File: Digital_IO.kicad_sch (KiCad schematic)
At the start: 27 parts, among them J1 MMCX, J10 MMCX, J11 MMCX, J12 MMCX, J13 MMCX, J14 MMCX, J15 MMCX, J16 MMCX, J2 MMCX, J3 MMCX, J4 MMCX, J5 MMCX, J6 MMCX, J7 MMCX, J8 MMCX, J9 MMCX, U45 TLV75901PDRV, U46 TLV75901PDRV

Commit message: Routed LVDS lines
- Routed LVDS lines
- Swapped some digital output pairs
- Properly connected the output enable signal for digital outputs in the schematic
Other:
- note removed: "TODO!: Need Level Translation through existing gate on u26/u27"
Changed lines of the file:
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@@
 		(comment 1 "SPDX-License-Identifier: CERN-OHL-S-2.0+")
 	)
-	(text "TODO!: Need Level Translation through existing gate\non u26/u27"
-		(exclude_from_sim no)
-		(at 115.062 72.39 0)
-		(effects
-			(font
-				(size 1.27 1.27)
-			)
-		)
-	)
 	(junction
 		(at 280.67 114.3)
@@
 	(wire
 		(pts
-			(xy 137.16 53.34) (xy 143.51 53.34)
+			(xy 59.69 161.29) (xy 59.69 158.75)
 		)
 		(stroke
@@
 		)
 	)
-	(wire
+	(bus
 		(pts
-			(xy 59.69 161.29) (xy 59.69 158.75)
+			(xy 43.18 83.82) (xy 43.18 86.36)
 		)
 		(stroke
@@
 		)
 	)
-	(bus
+	(wire
 		(pts
-			(xy 43.18 83.82) (xy 43.18 86.36)
+			(xy 175.26 91.44) (xy 181.61 91.44)
 		)
 		(stroke
@@
 	(wire
 		(pts
-			(xy 181.61 91.44) (xy 175.26 91.44)
+			(xy 175.26 92.71) (xy 173.99 92.71)
 		)
 		(stroke
@@
 		)
 	)
-	(wire
-		(pts
-			(xy 92.71 53.34) (xy 92.71 68.58)
-		)
-		(stroke
-			(width 0)
-			(type default)
-		)
-	)
 	(bus
 		(pts
@@
 	(wire
 		(pts
-			(xy 92.71 68.58) (xy 137.16 68.58)
+			(xy 224.79 44.45) (xy 243.84 44.45)
 		)
 		(stroke
@@
 	(wire
 		(pts
-			(xy 224.79 44.45) (xy 243.84 44.45)
+			(xy 162.56 25.4) (xy 181.61 25.4)
 		)
 		(stroke
@@
 	(wire
 		(pts
-			(xy 162.56 25.4) (xy 181.61 25.4)
+			(xy 30.48 16.51) (xy 64.77 16.51)
 		)
 		(stroke
@@
 	(wire
 		(pts
-			(xy 87.63 53.34) (xy 92.71 53.34)
+			(xy 30.48 19.05) (xy 64.77 19.05)
 		)
 		(stroke
@@
 	(wire
 		(pts
+			(xy 175.26 92.71) (xy 175.26 91.44)
+		)
+		(stroke
+			(width 0)
+			(type default)
+		)
+	)
+	(wire
+		(pts
 			(xy 64.77 40.64) (xy 45.72 40.64)
 		)
@@
 	(wire
 		(pts
-			(xy 137.16 53.34) (xy 137.16 68.58)
-		)
-		(stroke
-			(width 0)
-			(type default)
-		)
-	)
-	(wire
-		(pts
 			(xy 64.77 53.34) (xy 45.72 53.34)
 		)
@@
 		)
 	)
-	(label "OE"
-		(at 175.26 91.44 0)
+	(label "OE_A"
+		(at 64.77 16.51 180)
 		(effects
 			(font
 				(size 1.27 1.27)
 			)
-			(justify left bottom)
+			(justify right bottom)
 		)
 	)
@@
 		)
 	)
-	(label "OE"
+	(label "OE_B"
 		(at 237.49 57.15 0)
 		(effects
@@
 		)
 	)
+	(label "OE_A"
+		(at 175.26 38.1 0)
+		(effects
+			(font
+				(size 1.27 1.27)
+			)
+			(justify left bottom)
+		)
+	)
 	(label "D_Output6.N"
 		(at 64.77 55.88 180)
@@
 		)
 	)
-	(label "OE"
+	(label "OE_B"
 		(at 237.49 146.05 0)
 		(effects
@@
 		)
 	)
-	(label "OE"
+	(label "OE_B"
 		(at 237.49 92.71 0)
 		(effects
@@
 		)
 	)
-	(label "OE"
-		(at 175.26 127 0)
-		(effects
-			(font
-				(size 1.27 1.27)
-			)
-			(justify left bottom)
-		)
-	)
 	(label "VCC_B"
 		(at 236.22 17.78 0)
@@
 		)
 	)
-	(label "D_Output6.P"
-		(at 162.56 129.54 0)
+	(label "OE_A"
+		(at 173.99 92.71 0)
 		(effects
 			(font
@@
 		)
 	)
-	(label "OE"
-		(at 175.26 38.1 0)
+	(label "D_Output6.P"
+		(at 162.56 129.54 0)
 		(effects
 			(font
@@
 		)
 	)
-	(label "OE"
+	(label "OE_B"
 		(at 237.49 128.27 0)
 		(effects
@@
 		)
 	)
-	(label "OE"
-		(at 175.26 144.78 0)
-		(effects
-			(font
-				(size 1.27 1.27)
-			)
-			(justify left bottom)
-		)
-	)
 	(label "VCC_B"
 		(at 236.22 124.46 0)
@@
 		)
 	)
-	(label "OE"
-		(at 175.26 109.22 0)
-		(effects
-			(font
-				(size 1.27 1.27)
-			)
-			(justify left bottom)
-		)
-	)
 	(label "VCC_A"
 		(at 173.99 16.51 0)
@@
 		)
 	)
+	(label "OE_A"
+		(at 175.26 73.66 0)
+		(effects
+			(font
+				(size 1.27 1.27)
+			)
+			(justify left bottom)
+		)
+	)
 	(label "D_Output4.N"
 		(at 162.56 96.52 0)
@@
 		)
 	)
+	(label "OE_A"
+		(at 175.26 144.78 0)
+		(effects
+			(font
+				(size 1.27 1.27)
+			)
+			(justify left bottom)
+		)
+	)
 	(label "VCC_A"
 		(at 173.99 140.97 0)
@@
 		)
 	)
-	(label "OE"
-		(at 175.26 73.66 0)
-		(effects
-			(font
-				(size 1.27 1.27)
-			)
-			(justify left bottom)
-		)
-	)
 	(label "D_Output15.N"
 		(at 224.79 151.13 0)
@@
 		)
 	)
-	(label "OE"
+	(label "OE_B"
 		(at 237.49 110.49 0)
 		(effects
@@
 		)
 	)
-	(label "OE"
+	(label "OE_A"
 		(at 175.26 20.32 0)
 		(effects
@@
 		)
 	)
-	(label "OE"
-		(at 143.51 53.34 180)
+	(label "OE_B"
+		(at 64.77 19.05 180)
 		(effects
 			(font
@@
 		)
 	)
+	(label "OE_A"
+		(at 175.26 109.22 0)
+		(effects
+			(font
+				(size 1.27 1.27)
+			)
+			(justify left bottom)
+		)
+	)
 	(label "D_Output15.P"
 		(at 64.77 99.06 180)
@@
 		)
 	)
-	(label "OE"
+	(label "OE_B"
 		(at 237.49 74.93 0)
 		(effects
@@
 		)
 	)
-	(label "OE"
-		(at 175.26 55.88 0)
+	(label "D_Output1.N"
+		(at 162.56 43.18 0)
 		(effects
 			(font
@@
 		)
 	)
-	(label "D_Output1.N"
-		(at 162.56 43.18 0)
+	(label "D_Output7.P"
+		(at 64.77 58.42 180)
+		(effects
+			(font
+				(size 1.27 1.27)
+			)
+			(justify right bottom)
+		)
+	)
+	(label "OE_A"
+		(at 175.26 127 0)
 		(effects
 			(font
@@
 		)
 	)
-	(label "D_Output7.P"
-		(at 64.77 58.42 180)
+	(label "OE_A"
+		(at 175.26 55.88 0)
 		(effects
 			(font
 				(size 1.27 1.27)
 			)
-			(justify right bottom)
+			(justify left bottom)
 		)
 	)
@@
 		)
 	)
-	(label "OE"
+	(label "OE_B"
 		(at 237.49 21.59 0)
 		(effects
@@
 		)
 	)
-	(label "OE"
+	(label "OE_B"
 		(at 237.49 39.37 0)
 		(effects
@@
 		)
 	)
-	(hierarchical_label "OE"
+	(hierarchical_label "OE_B"
+		(shape input)
+		(at 30.48 19.05 180)
+		(effects
+			(font
+				(size 1.27 1.27)
+			)
+			(justify right)
+		)
+	)
+	(hierarchical_label "OE_A"
 		(shape input)
-		(at 87.63 53.34 180)
+		(at 30.48 16.51 180)
 		(effects
 			(font

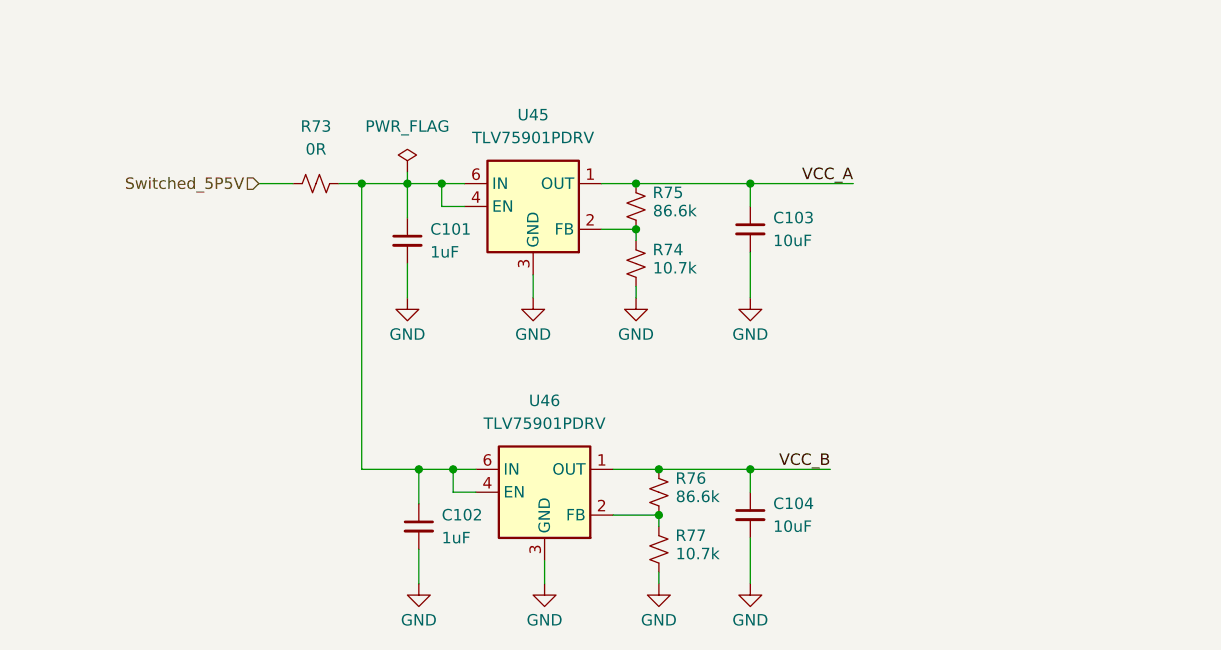
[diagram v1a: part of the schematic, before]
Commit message: Finished Draft Layout
- Finished Draft Layout
- Changed Switcher IC
- Added extra decoupling caps for digital output spikes
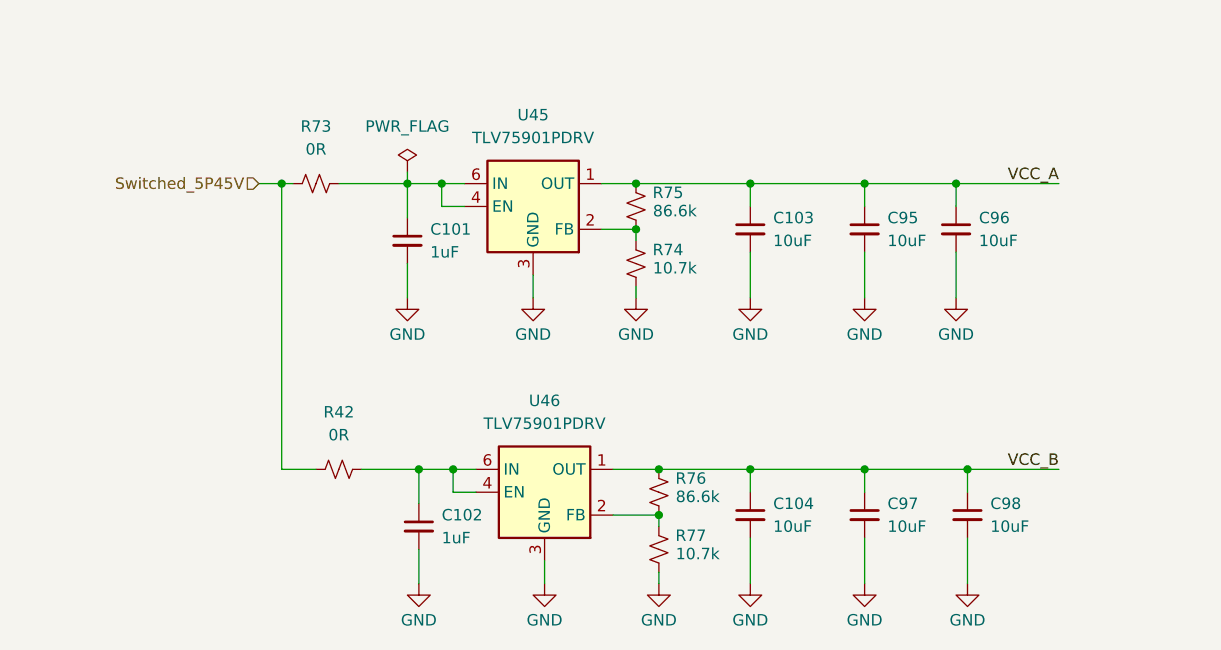
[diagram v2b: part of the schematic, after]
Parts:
- added C95, C96, C97, C98: 10uF, Capacitor_SMD:C_0805_2012Metric, symbol Device:C_Small
- added R42: 0R, Resistor_SMD:R_0603_1608Metric, symbol Device:R_Small_US
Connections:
- net GND: now also C95.2, C96.2, C97.2, C98.2
- net VCC_A: now also C95.1, C96.1
- net VCC_B: now also C97.1, C98.1
- net at C101.1, R73.2, U45.4 (EN)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: no longer C102.1, U46.4 (EN), U46.6 (IN)
- net Switched_5P5V renamed Switched_5P45V
- net Switched_5P45V: now also R42.1
- new net: C102.1, R42.2, U46.4 (EN), U46.6 (IN)

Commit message: Fixed Silkscreen and BOM
All DRC/ERC errors are resolved.
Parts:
- C101, C102: Comment CAP CER 1UF 16V X7R 0603 -> (none); Designator C6 -> (none); Digikey (none) -> 490-5241-6-ND; LCSC C161212 -> (none)
- C103, C104, C95, C96, C97, C98: Comment CAP CER 10UF 25V X5R 0805 -> (none); Designator C7 -> (none); Digikey (none) -> 490-5523-6-ND; LCSC C84416 -> (none)
- J1, J10, J11, J12, J13, J14, J15, J16, J2, J3, J4, J5, J6, J7, J8, J9: Digikey (none) -> SAM10617-ND
- R42, R73: Digikey (none) -> P0.0GDKR-ND
- R74, R77: Digikey (none) -> 13-RC0402FR-1310K7LDKR-ND; MPN (none) -> RC0402FR-1310K7L
- R75, R76: Digikey (none) -> YAG3249DKR-ND; MPN (none) -> RC0402FR-0786K6L
- U45, U46: Digikey (none) -> 296-TLV75901PDRVRDKR-ND; MPN (none) -> TLV75901PDRVR; Manufacturer (none) -> Texas Instruments
